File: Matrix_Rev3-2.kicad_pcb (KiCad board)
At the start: 2 copper layers, 193 x 156.2 mm, 34 parts, among them SW1 DPST, SW10 DPST, SW11 DPST, SW12 DPST, SW13 DPST, SW14 DPST, SW15 DPST, SW16 DPST, SW2 DPST, SW3 DPST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

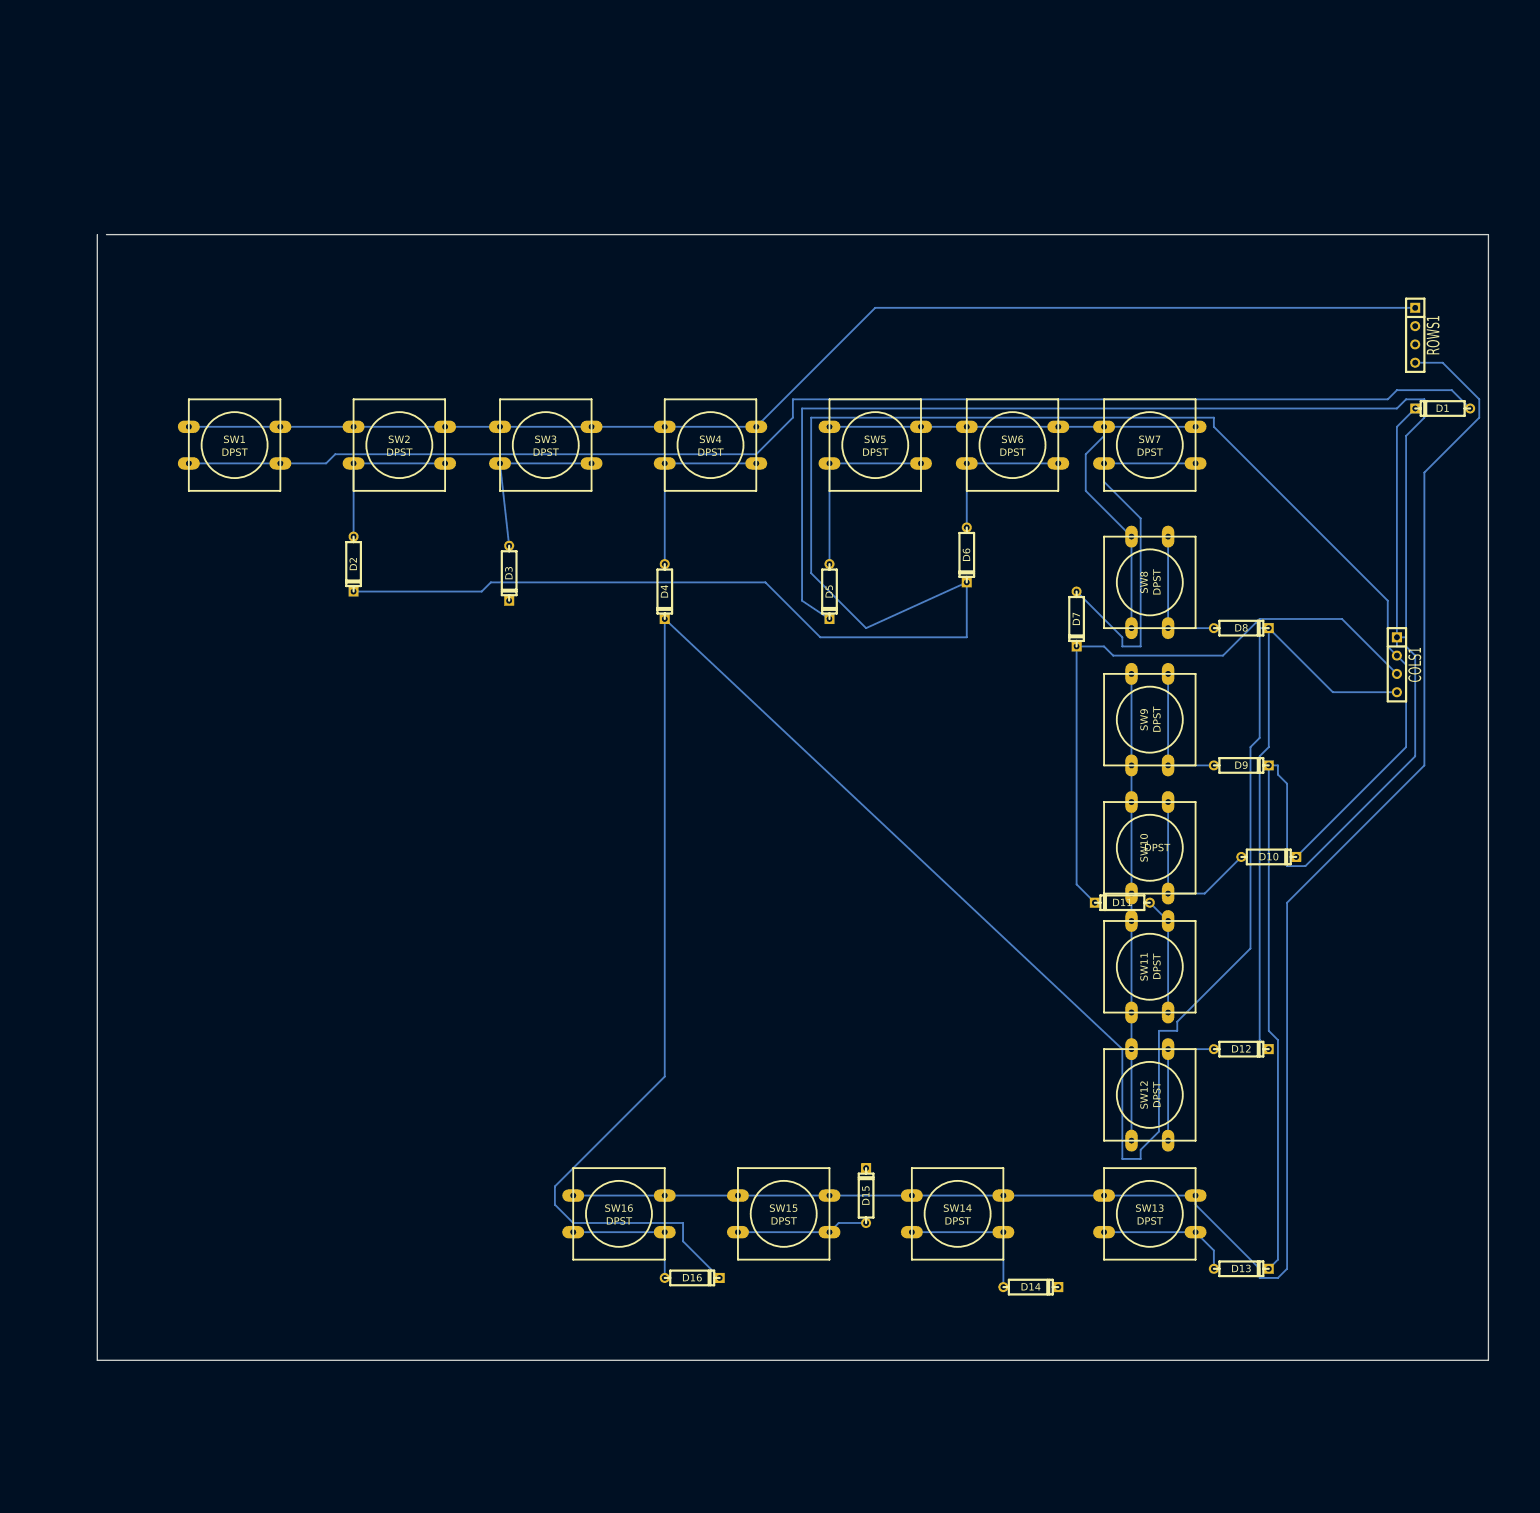
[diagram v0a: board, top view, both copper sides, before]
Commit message: First schematic with pots
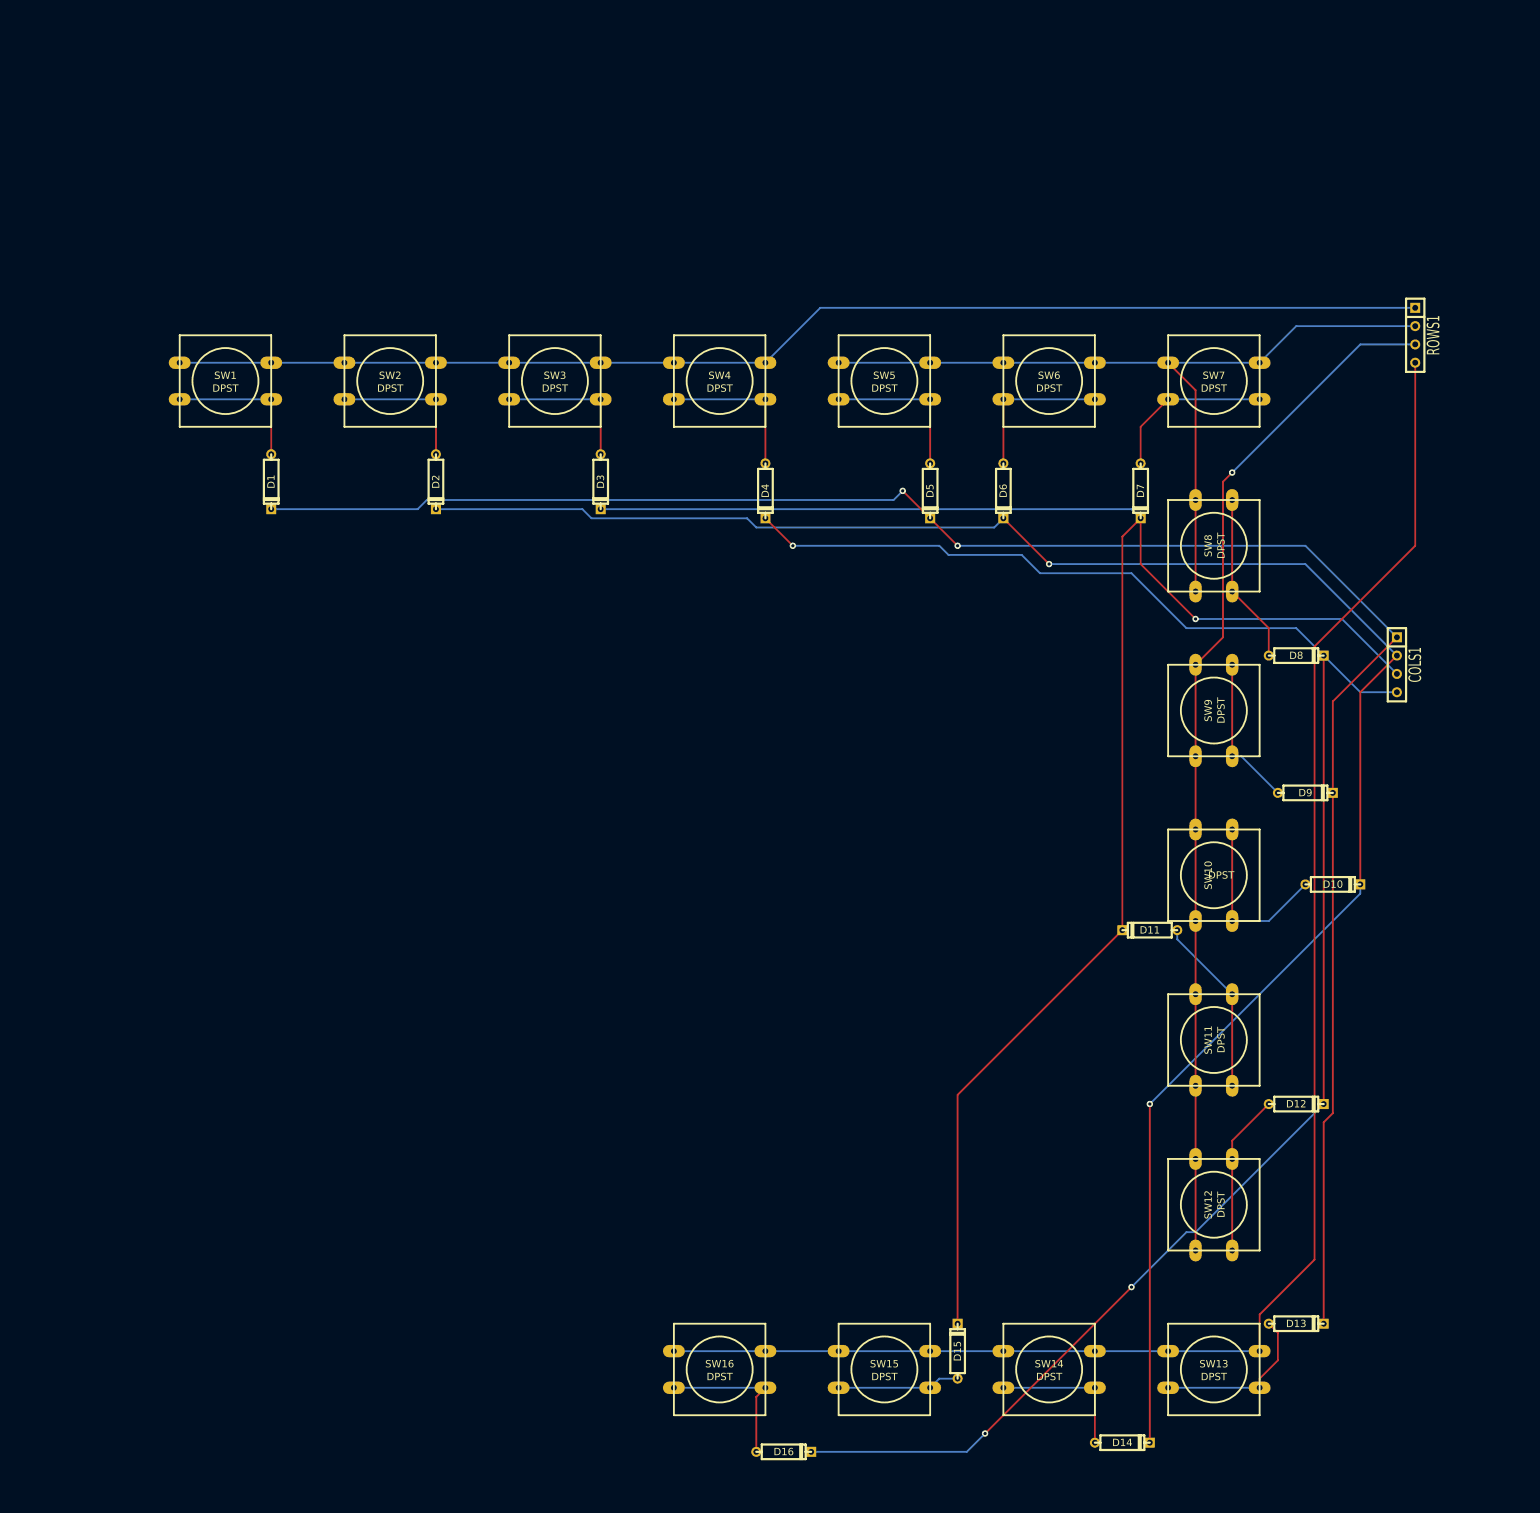
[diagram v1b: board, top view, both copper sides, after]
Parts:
- moved D1 162.9 mm to (185.4, 116.8), turned to 270 degrees
- moved D16 27.3 mm to (256.5, 251.5)
- moved SW16 25.7 mm to (247.7, 240.0)
- moved SW15 25.7 mm to (270.5, 240.0)
- moved D14 25.0 mm to (303.5, 250.2)
- moved D15 25.0 mm to (280.7, 237.5)
- moved SW14 25.0 mm to (293.4, 240.0)
- moved SW13 23.3 mm to (316.2, 240.0)
- moved D7 19.9 mm to (306.1, 118.1)
- moved D5 19.8 mm to (276.9, 118.1)
- moved D4 19.8 mm to (254.0, 118.1)
- moved D3 18.0 mm to (231.1, 116.8)
- moved SW12 17.6 mm to (316.2, 217.2)
- moved D2 16.2 mm to (208.3, 116.8)
- moved SW11 13.5 mm to (316.2, 194.3)
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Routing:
- net N-0000014: track 184.5 -> 20.3 mm
- net /c3: track 86.8 -> 246.0 mm, vias 0 -> 1
- net /c4: track 385.3 -> 251.0 mm, vias 0 -> 3
- net /a3: track 64.8 -> 142.8 mm, vias 0 -> 1
- net /c1: track 315.3 -> 265.1 mm, vias 0 -> 2
- net /a2: track 82.4 -> 115.4 mm
- net N-0000022: track 53.0 -> 23.2 mm
- net /a4: track 248.5 -> 227.4 mm
- net /c2: track 278.3 -> 266.2 mm, vias 0 -> 2
- net N-000007: track 16.3 -> 24.7 mm
- net N-0000024: track 26.7 -> 21.6 mm
- net N-0000019: track 26.7 -> 21.6 mm
- net N-0000023: track 19.1 -> 23.7 mm
- net N-0000012: track 18.8 -> 23.2 mm
- net N-0000018: track 24.2 -> 20.3 mm
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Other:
- board outline removed

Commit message: New libary files etc
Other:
- board outline added: 209.6 x 205.7 mm
